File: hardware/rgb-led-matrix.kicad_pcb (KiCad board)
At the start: 2 copper layers, 75 x 55 mm, 160 parts, among them J1 AKL_5_2, P1 CONN_01X02, P2 CON-SENSOR, Q1 2N7002P, U1 XMC1100-16, U2 DRILL, U3 DRILL, U4 DRILL, U5 DRILL

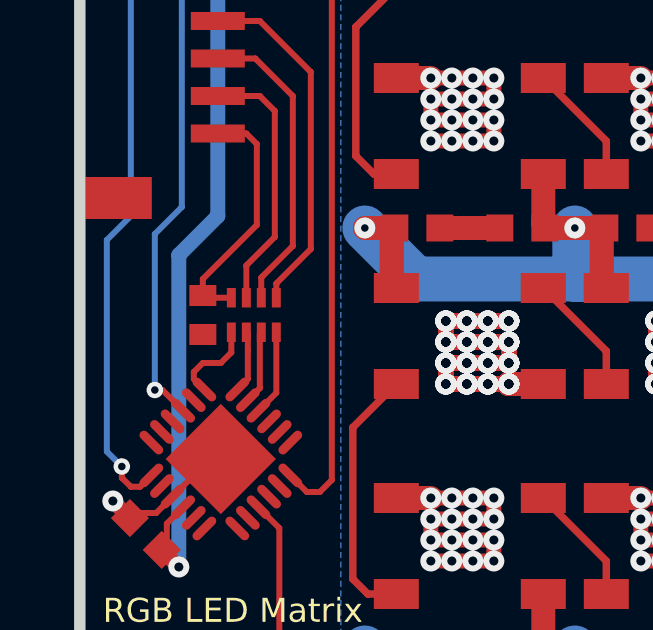
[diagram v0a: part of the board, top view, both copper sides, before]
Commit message: Change capacitor footprint(s) to C0402F
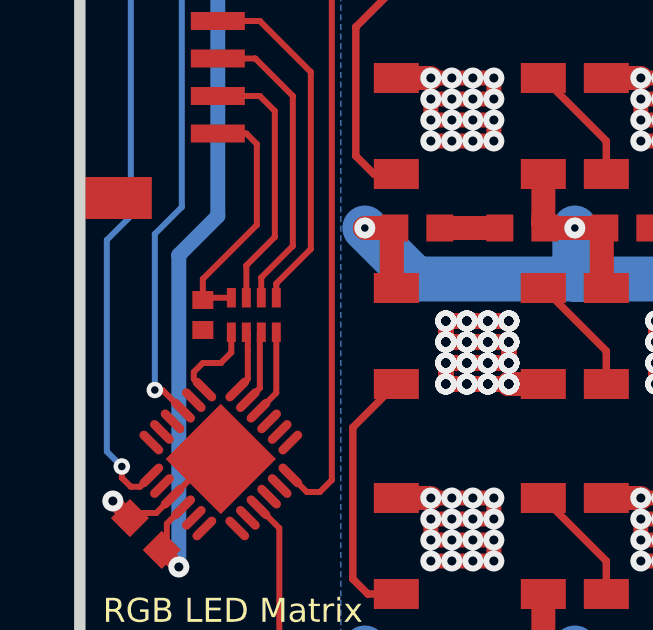
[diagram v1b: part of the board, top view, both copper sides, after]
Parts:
- C70: footprint kicad-libraries:C0402E -> kicad-libraries:C0402F
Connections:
- LED64 pad 2: (no net) -> Net-(LED64-Pad2)
- P2 pad 1: (no net) -> Net-(P2-Pad1)
- R2 pad 1: Net-(Q1-PadD) -> Net-(R2-Pad1)
- R3 pad 1: Net-(Q1-PadG) -> Net-(R3-Pad1)
- R4 pad 2: Net-(Q1-PadD) -> Net-(R2-Pad1)
- U1 pad 11: (no net) -> Net-(U1-Pad11)
- U1 pad 12: (no net) -> Net-(U1-Pad12)
- U1 pad 13: (no net) -> Net-(U1-Pad13)
- U1 pad 14: (no net) -> Net-(U1-Pad14)
- U1 pad 16: (no net) -> Net-(U1-Pad16)
- U1 pad 17: (no net) -> Net-(U1-Pad17)
- U1 pad 19: (no net) -> Net-(U1-Pad19)
- U1 pad 2: (no net) -> Net-(U1-Pad2)
- U1 pad 20: (no net) -> Net-(U1-Pad20)
- U1 pad 21: (no net) -> Net-(U1-Pad21)
- U1 pad 4: (no net) -> Net-(U1-Pad4)
- U1 pad 5: (no net) -> Net-(U1-Pad5)
- U1 pad 6: (no net) -> Net-(U1-Pad6)
- U1 pad 8: (no net) -> Net-(U1-Pad8)
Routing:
- net Net-(R2-Pad1): track 0.00 -> 2.59 mm
- net Net-(Q1-PadD): track 5.06 -> 2.47 mm
- net Net-(R3-Pad1): track 0.00 -> 1.42 mm
- net Net-(Q1-PadG): track 1.44 -> 0.02 mm
